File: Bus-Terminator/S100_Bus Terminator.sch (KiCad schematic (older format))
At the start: 70 parts, among them IC1 7805, IC2 LM4250, P1 S100_MALE, P16 CONN_2, P2 CONN_4, P3 CONN_4, P34 CONN_1, P35 CONN_1, Q1 2N3906, Q2 2N3904, Q3 TIP29, Q4 TIP30, Q5 2N3904, Q6 2N3904, Q7 2N3904, SW1 SW_PUSH, U1 LDO_REG_7805, U2 74LS04

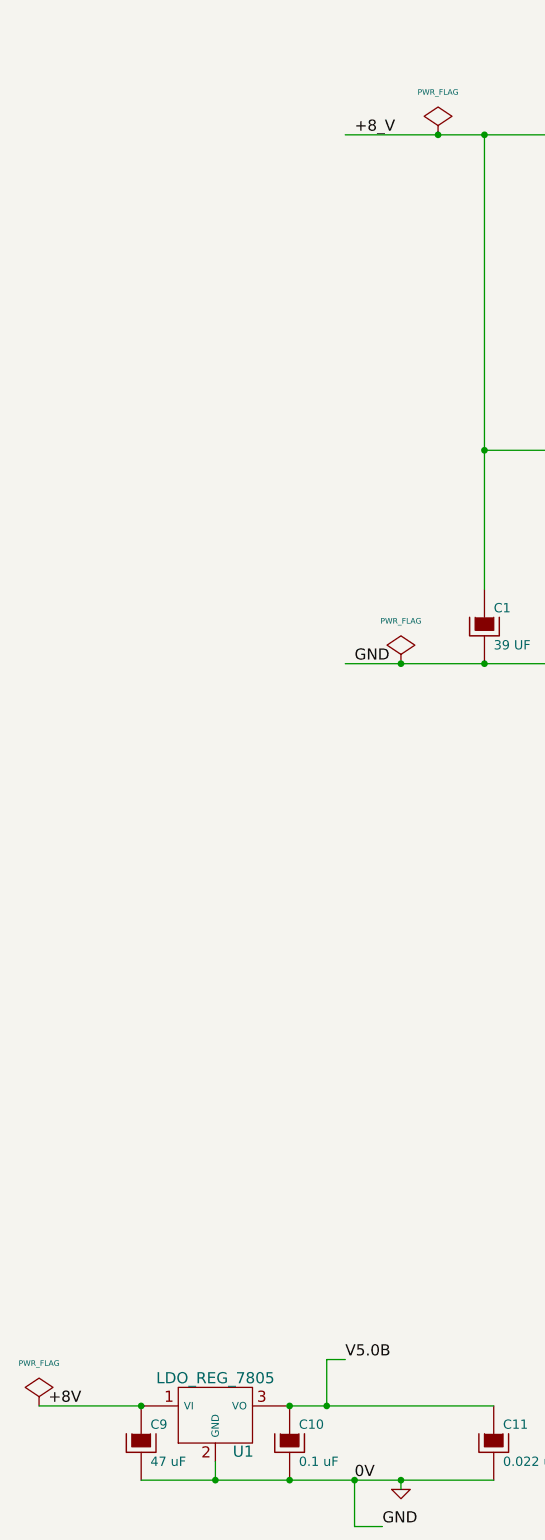
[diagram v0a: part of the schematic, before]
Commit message: Bus-Terminator: tidy power flags, re-place parts (unrouted)
Source: S100 Bus Terminator v1/backups/03-08-2014 1204
Removed a spare PWR_FLAG and label; parts moved on the board, still unrouted.
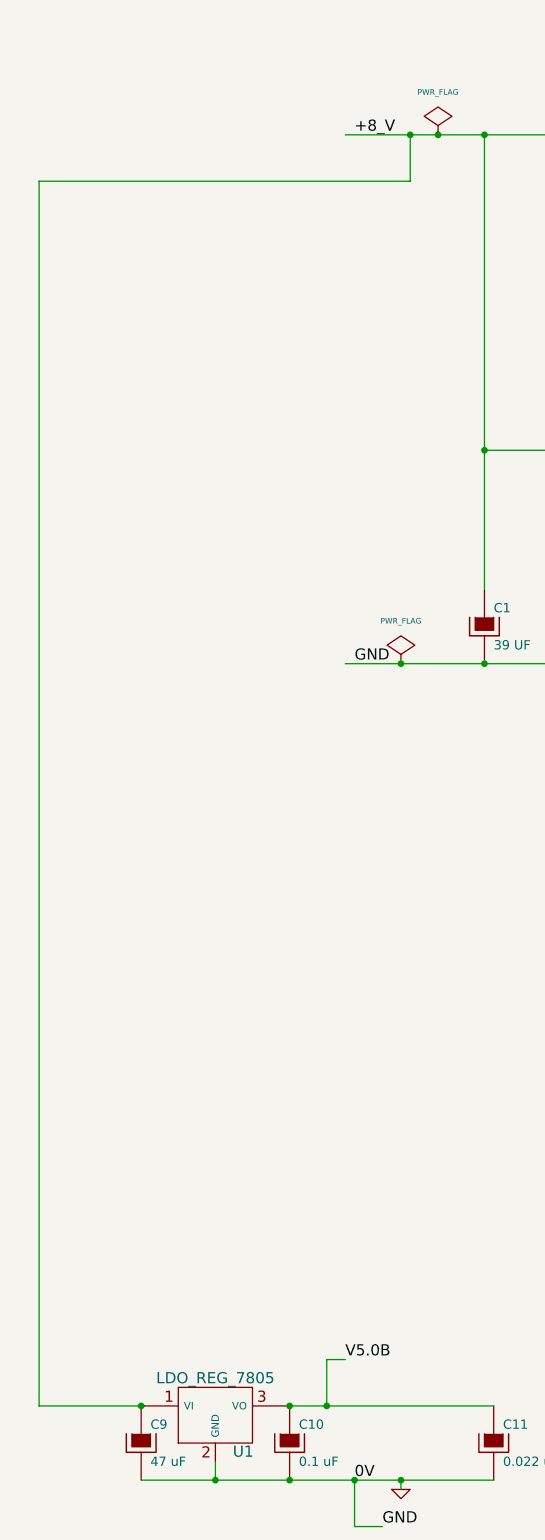
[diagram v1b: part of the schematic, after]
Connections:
- net labels removed: +8V
- wire segments 336 -> 339
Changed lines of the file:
@@
 Sheet 1 1
 Title "noname.sch"
-Date "2 aug 2014"
+Date "3 aug 2014"
 Rev ""
 Comp ""
@@
 	1    0    0    -1
 $EndComp
-Text Label 950  11850 0    60   ~ 0
-+8V
 $Comp
 L CP C10
@@
 F 3 "" H 1450 12050 60  0001 C CNN
 	1    1450 12050
-	1    0    0    -1
-$EndComp
-$Comp
-L PWR_FLAG #FLG06
-U 1 1 53DD7D5A
-P 900 11850
-F 0 "#FLG06" H 900 12120 30  0001 C CNN
-F 1 "PWR_FLAG" H 900 12080 30  0000 C CNN
-F 2 "" H 900 11850 60  0001 C CNN
-F 3 "" H 900 11850 60  0001 C CNN
-	1    900  11850
 	1    0    0    -1
 $EndComp
@@
 Connection ~ 5200 10700
 NoConn ~ 5350 10600
+Wire Wire Line
+	900  11850 900  5250
+Wire Wire Line
+	900  5250 2900 5250
+Wire Wire Line
+	2900 5250 2900 5000
+Connection ~ 2900 5000
 $EndSCHEMATC

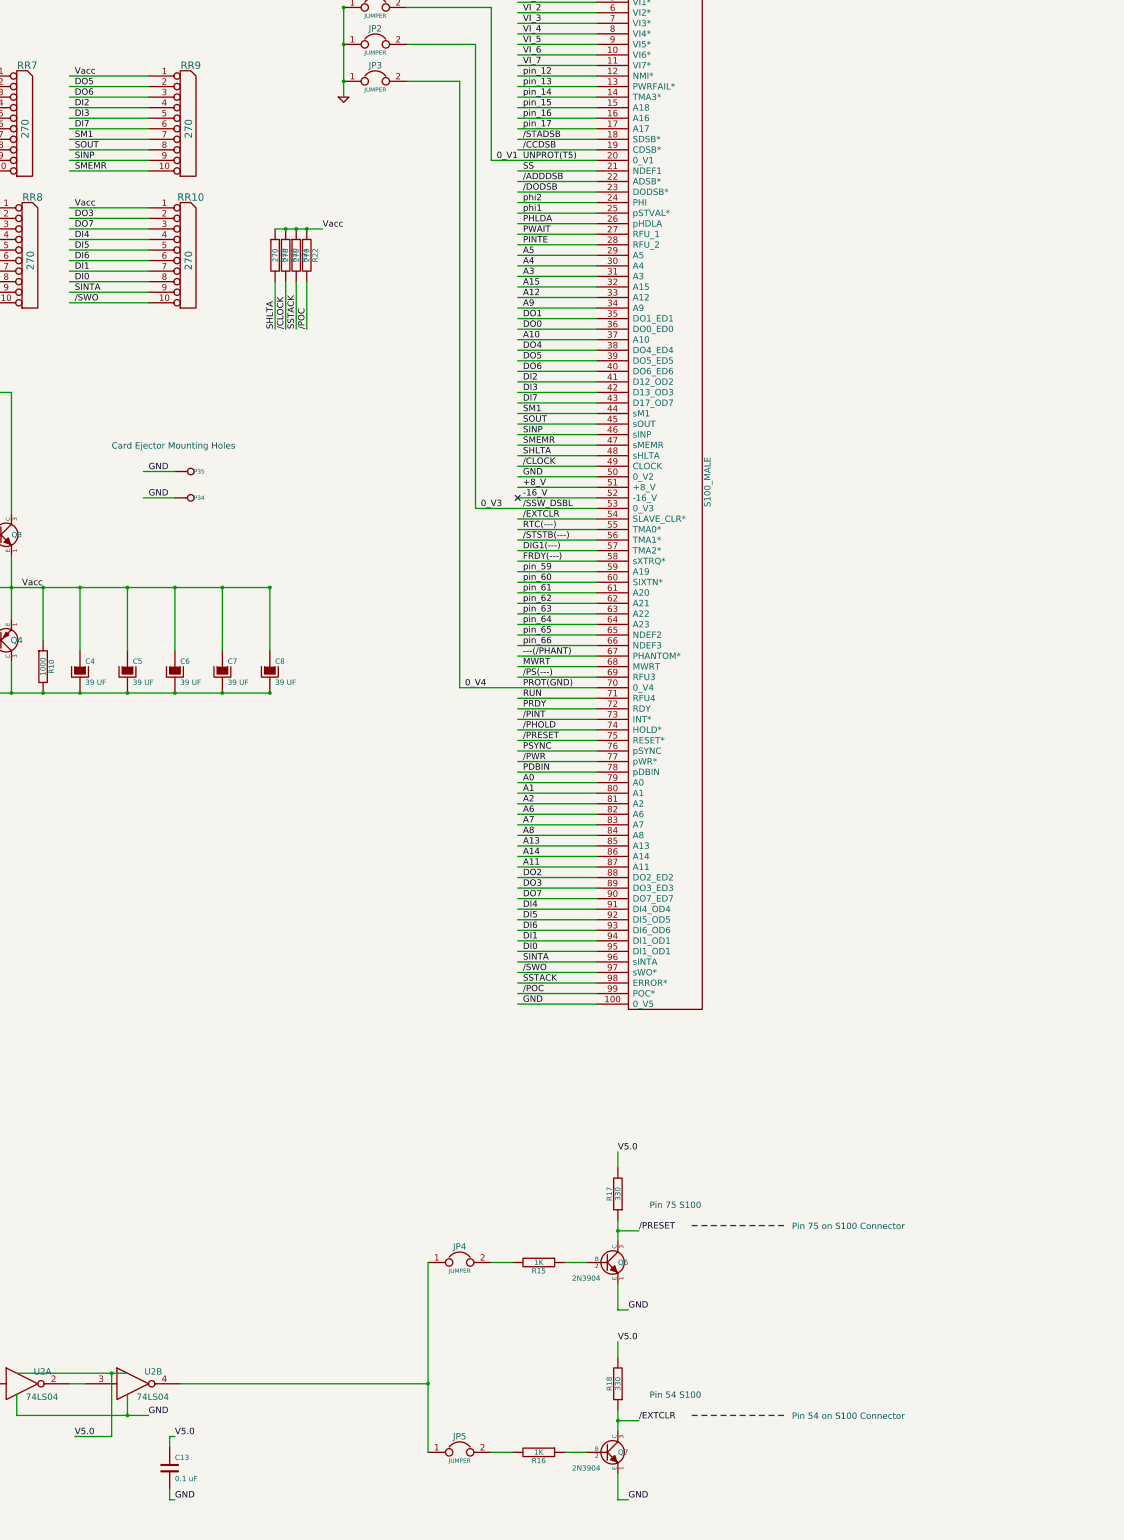
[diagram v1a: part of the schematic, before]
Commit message: Bus-Terminator: PRESET/EXTCLR jumpers JP6/JP7, routed board, gerbers
Source: S100 Bus Terminator v1 (working folder) and S100 Bus Terminator v1/GERBERS
Adds JP6/JP7, mounting holes, copper/silk text; 2-layer routing with GND pours; fab gerbers and drill file.
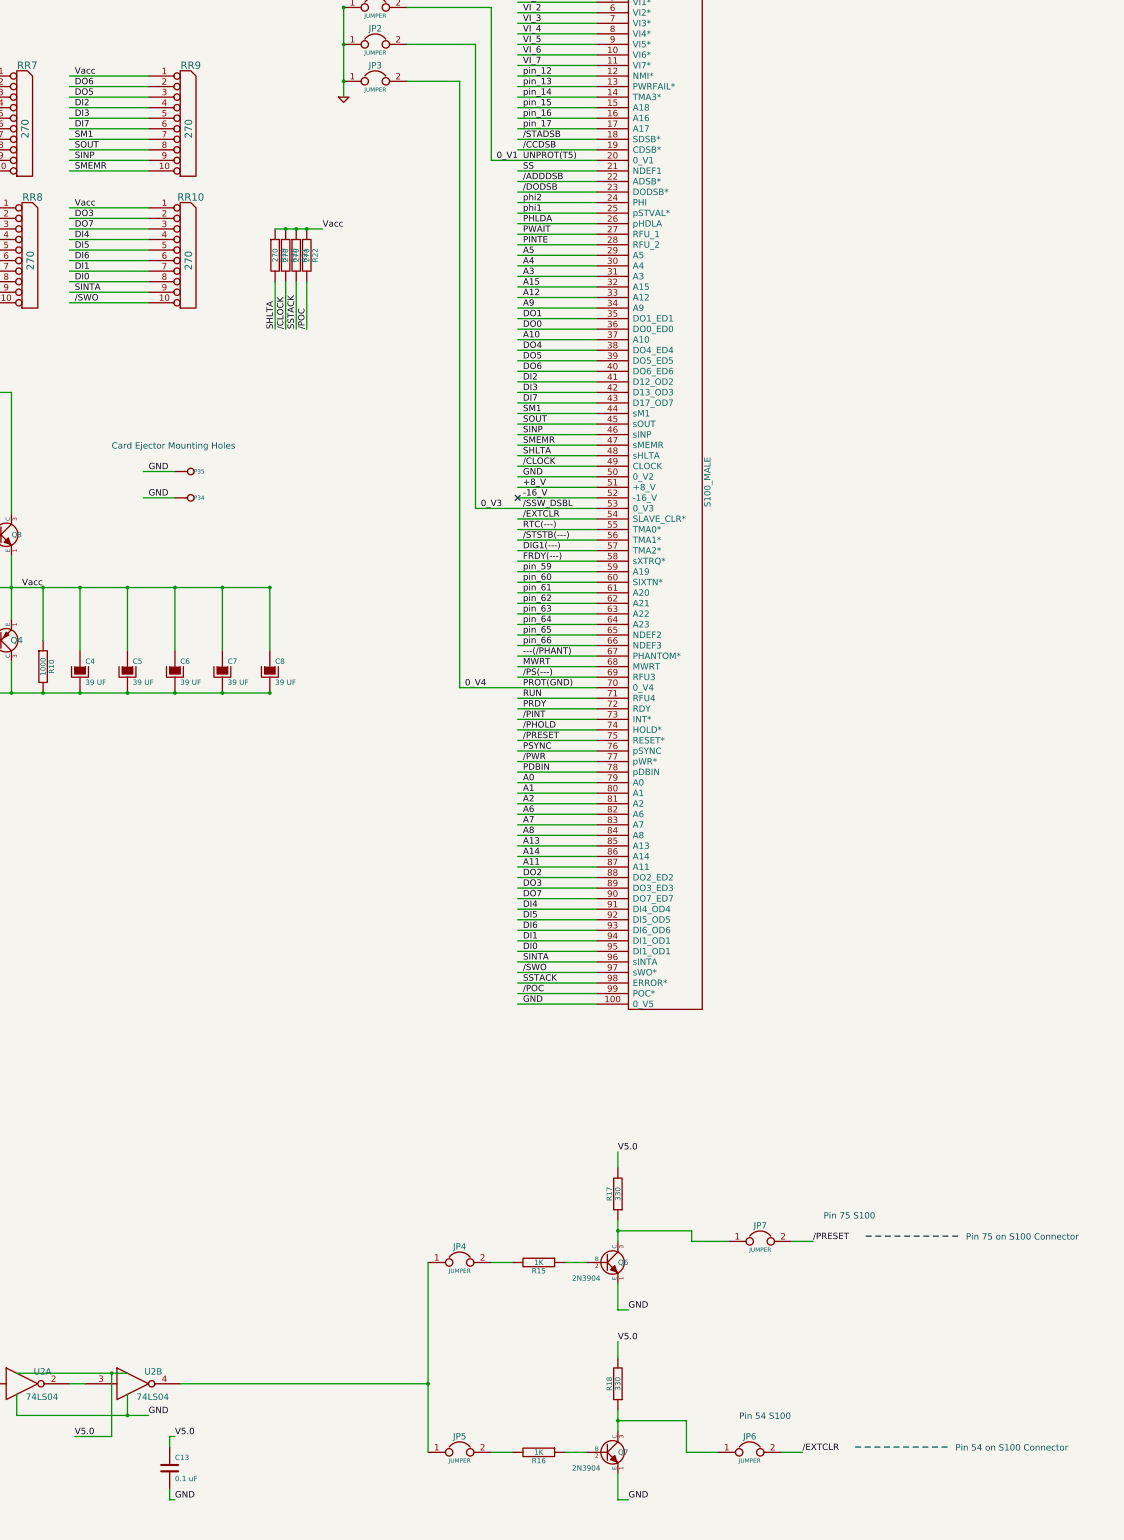
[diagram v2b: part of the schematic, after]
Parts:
- added JP6, JP7: JUMPER, SIL-2, symbol JUMPER
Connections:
- wire segments 339 -> 345
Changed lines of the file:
@@
 Text Label 8800 2300 0    60   ~ 0
 DI2
+Text Label 8800 2100 0    60   ~ 0
+DO6
 Text Label 8800 2200 0    60   ~ 0
-DO6
-Text Label 8800 2100 0    60   ~ 0
 DO5
 Text Label 7250 2900 0    60   ~ 0
@@
 	0    1    1    0
 $EndComp
-Text Label 14150 14750 0    60   ~ 0
+Text Label 15700 15050 0    60   ~ 0
 /EXTCLR
-Text Label 14150 12950 0    60   ~ 0
+Text Label 15800 13050 0    60   ~ 0
 /PRESET
 $Comp
@@
 	0    1    1    0
 $EndComp
-Text Notes 15600 14750 0    60   ~ 0
+Text Notes 17150 15050 0    60   ~ 0
 Pin 54 on S100 Connector
-Text Notes 15600 12950 0    60   ~ 0
+Text Notes 17250 13050 0    60   ~ 0
 Pin 75 on S100 Connector
 Wire Wire Line
@@
 	7000 14400 7850 14400
 Wire Notes Line
-	14650 12900 15550 12900
+	16300 13000 17200 13000
 $Comp
 L 74LS04 U2
@@
 Wire Wire Line
 	13450 13250 13650 13250
-Text Notes 14250 12750 0    60   ~ 0
+Text Notes 15900 12850 0    60   ~ 0
 Pin 75 S100
 Wire Wire Line
-	13950 12950 14150 12950
+	13950 12950 14650 12950
 Connection ~ 13950 12950
 Wire Notes Line
-	14650 14700 15550 14700
+	16200 15000 17100 15000
 $Comp
 L NPN Q7
@@
 Wire Wire Line
 	13450 15050 13650 15050
-Text Notes 14250 14550 0    60   ~ 0
+Text Notes 15100 14750 0    60   ~ 0
 Pin 54 S100
 Wire Wire Line
-	13950 14750 14150 14750
+	13950 14750 14600 14750
 Connection ~ 13950 14750
 $Comp
@@
 	2900 5250 2900 5000
 Connection ~ 2900 5000
+$Comp
+L JUMPER JP7
+U 1 1 53DD8BB4
+P 15300 13050
+F 0 "JP7" H 15300 13200 60  0000 C CNN
+F 1 "JUMPER" H 15300 12970 40  0000 C CNN
+F 2 "SIL-2" H 15300 13070 40  0001 C CNN
+F 3 "" H 15300 13050 60  0001 C CNN
+	1    15300 13050
+	1    0    0    -1
+$EndComp
+$Comp
+L JUMPER JP6
+U 1 1 53DD8BBA
+P 15200 15050
+F 0 "JP6" H 15200 15200 60  0000 C CNN
+F 1 "JUMPER" H 15200 14970 40  0000 C CNN
+F 2 "SIL-2" H 15200 15070 40  0001 C CNN
+F 3 "" H 15200 15050 60  0001 C CNN
+	1    15200 15050
+	1    0    0    -1
+$EndComp
+Wire Wire Line
+	14600 14750 14600 15050
+Wire Wire Line
+	14600 15050 14900 15050
+Wire Wire Line
+	15700 15050 15500 15050
+Wire Wire Line
+	15800 13050 15600 13050
+Wire Wire Line
+	14650 12950 14650 13050
+Wire Wire Line
+	14650 13050 15000 13050
 $EndSCHEMATC
